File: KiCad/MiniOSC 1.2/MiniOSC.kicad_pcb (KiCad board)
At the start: 2 copper layers, 94.1 x 128.5 mm, 58 parts, among them J1 Conn_01x16_Female, J2 Conn_01x16_Male, J3 V_OCT_IN, J4 FM_IN, J5 PULSE_OUT, J6 SAW_OUT, J7 JST_BUS, J8 IDC_BUS, Q1 BC558, Q2 BC548, U1 TL074, U2 40106

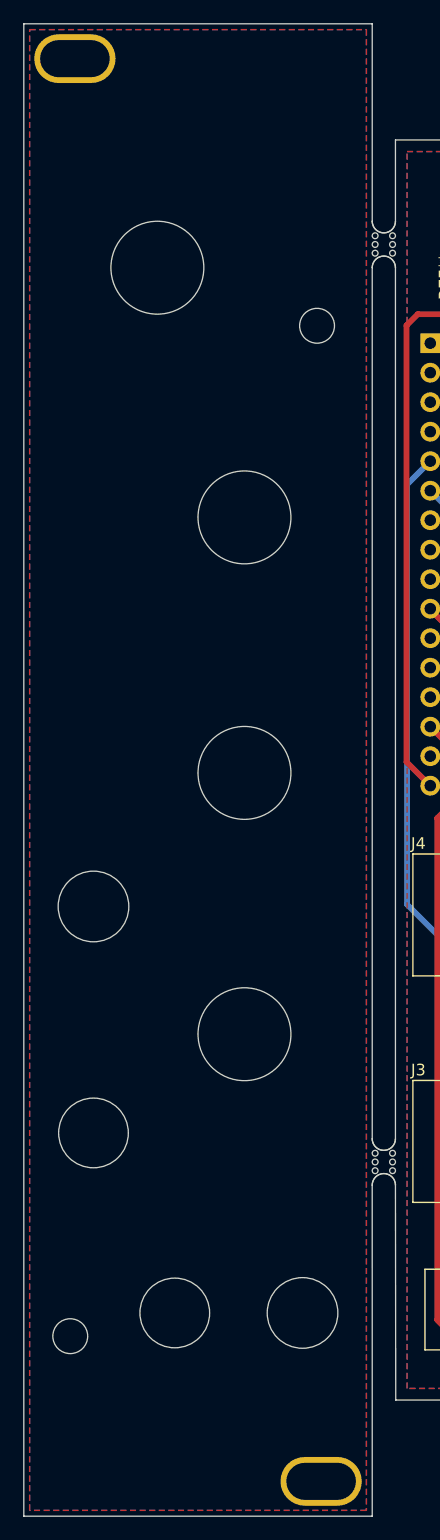
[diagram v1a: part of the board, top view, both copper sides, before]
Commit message: Updated labels
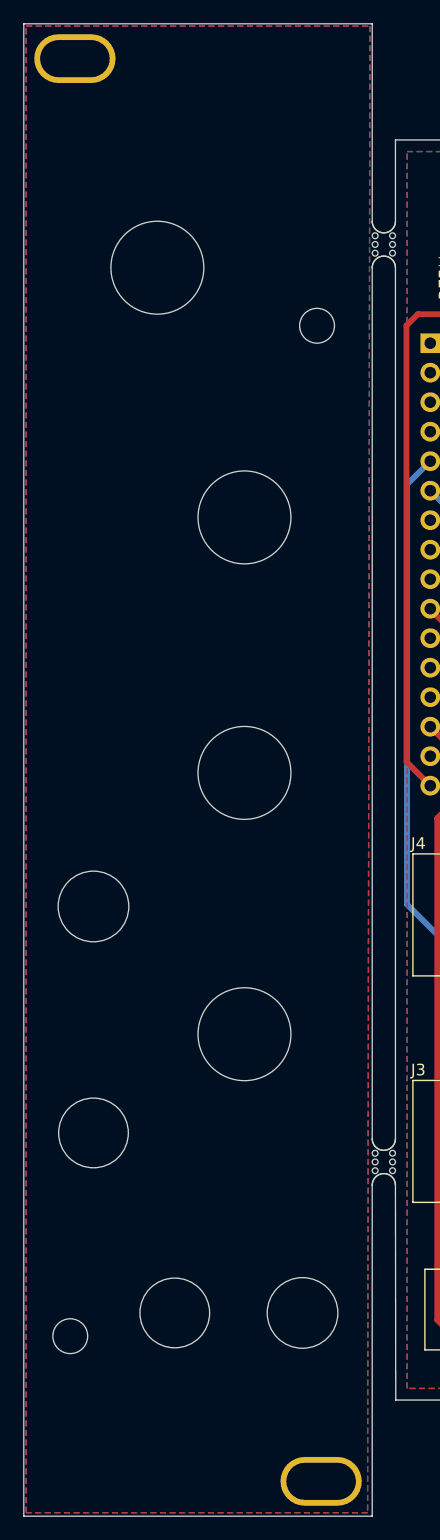
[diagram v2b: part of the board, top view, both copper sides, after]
